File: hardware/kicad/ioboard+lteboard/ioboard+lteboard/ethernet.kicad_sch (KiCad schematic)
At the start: 27 parts, among them T1 WE-RJ45_7499010441, U18 W5500, Y1 25MHz

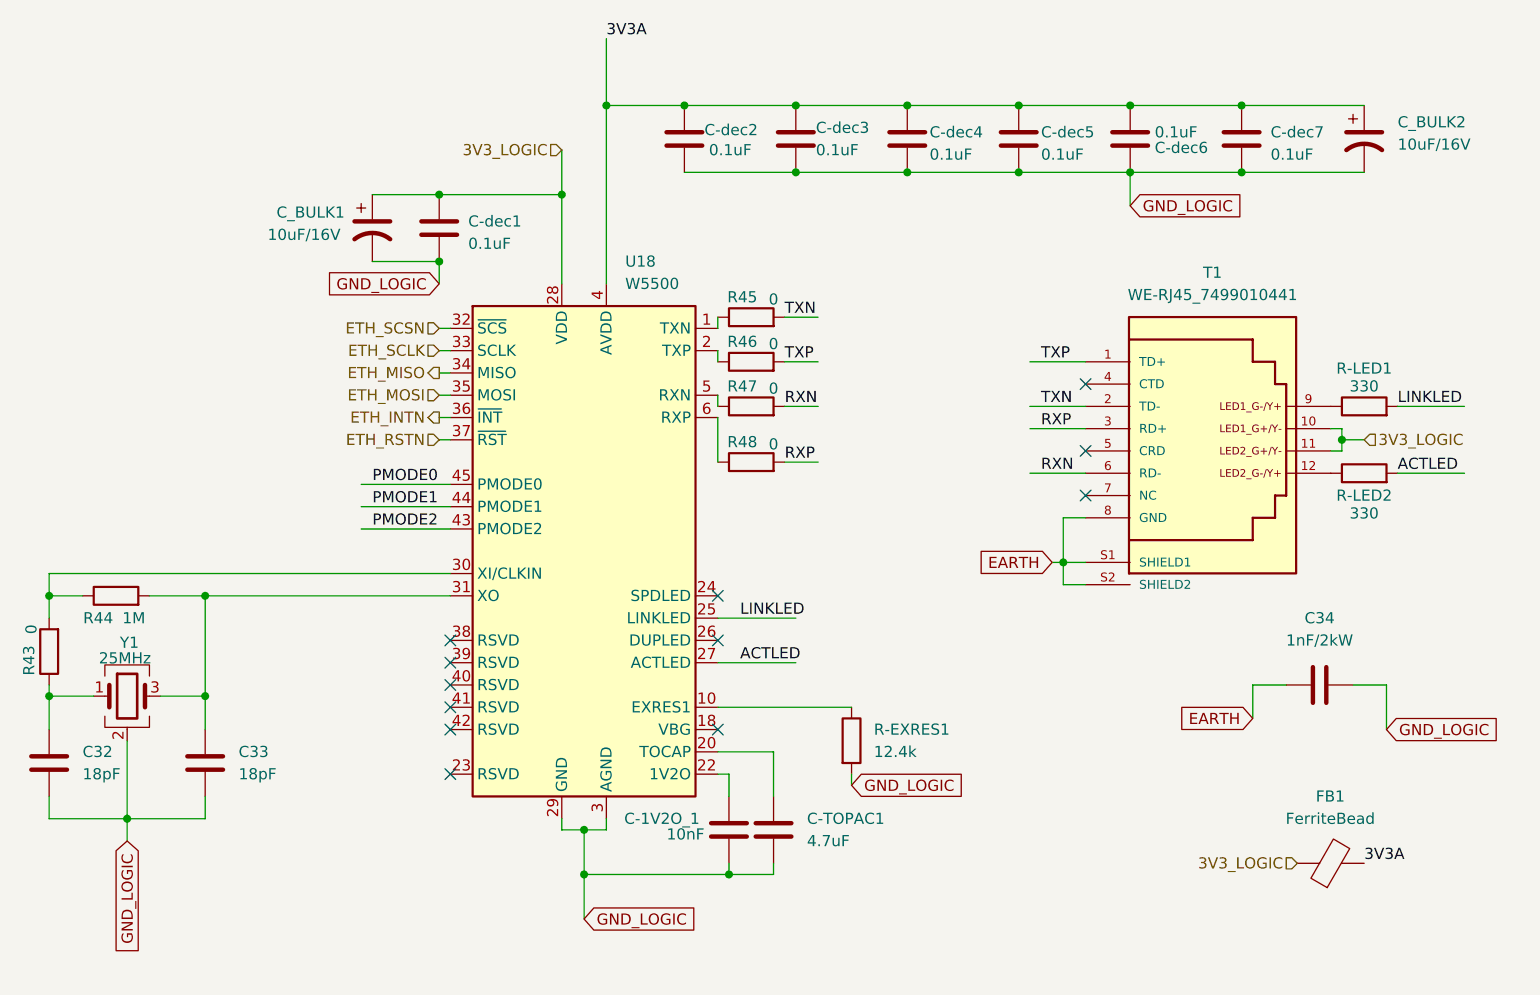
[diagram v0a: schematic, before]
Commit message: Close roadmap steps 6/7: pin assignment, board-to-board wiring, ERC pass clean; update docs to match
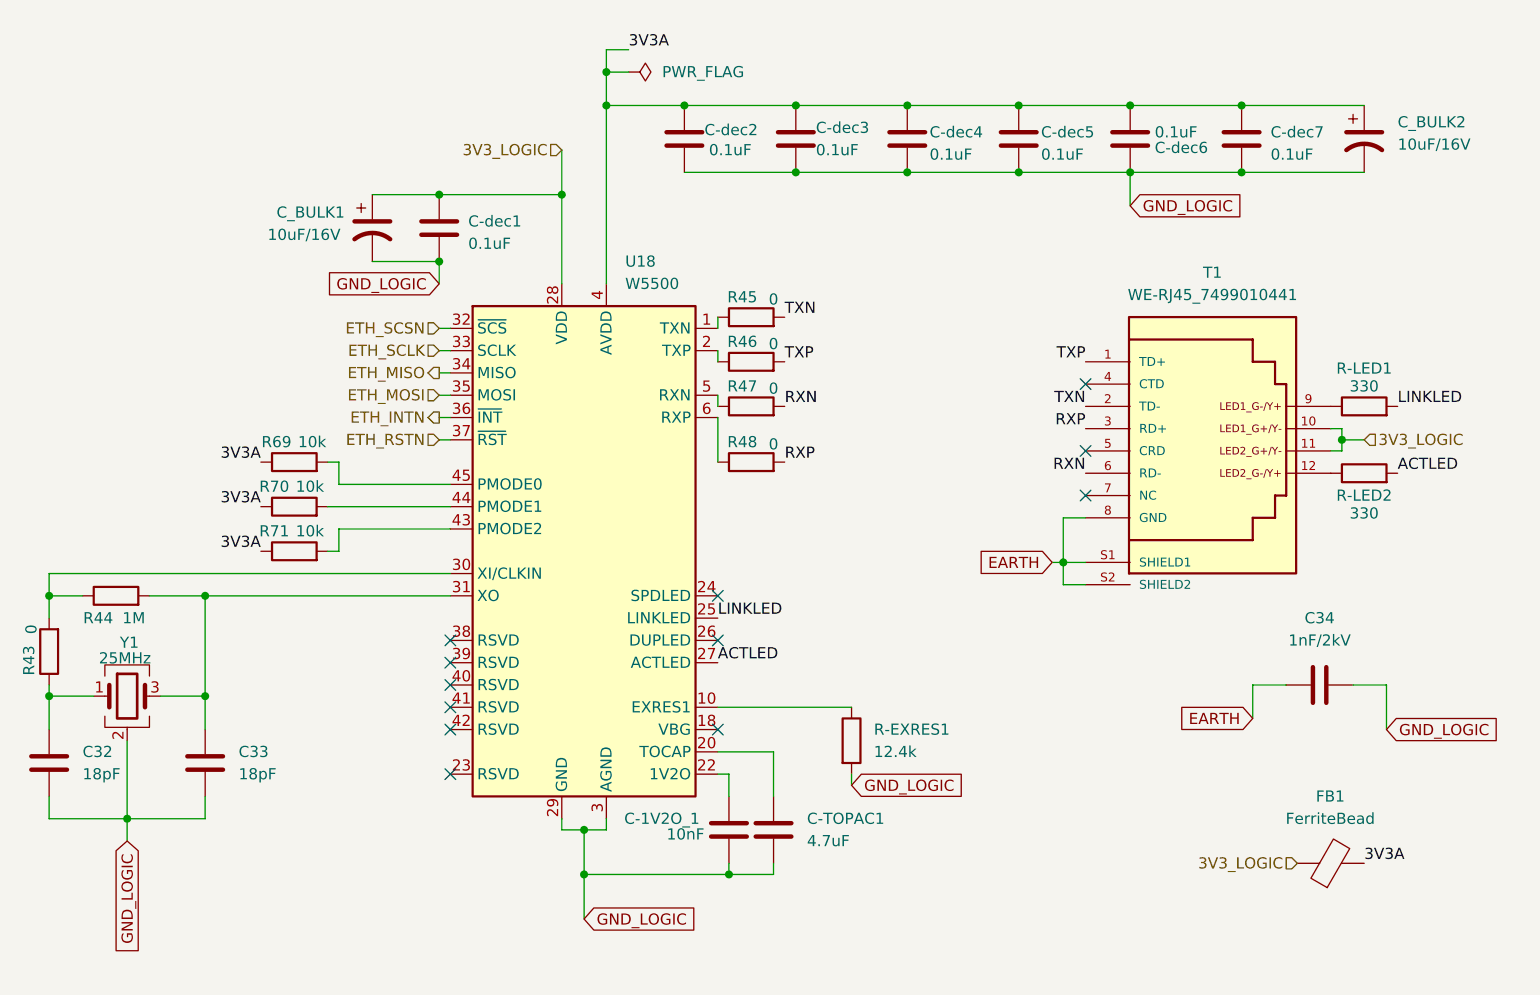
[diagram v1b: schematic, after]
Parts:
- added R69, R70, R71: 10k, symbol Device:R
- C34: value 1nF/2kW -> 1nF/2kV
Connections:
- net 3V3A: now also R69.1, R70.1, R71.1
- net PMODE0: no longer names the net of U18.45 (PMODE0)
- net PMODE0: now also R69.2
- net PMODE1: no longer names the net of U18.44 (PMODE1)
- net PMODE1: now also R70.2
- net PMODE2: no longer names the net of U18.43 (PMODE2)
- net PMODE2: now also R71.2
